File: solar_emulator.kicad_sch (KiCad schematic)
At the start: 37 parts, among them J1 USB_C_Receptacle, Q1 NMOS, Q2 NMOS, Q4 NMOS, Q5 NMOS, SW1 SW_Push, SW2 SW_Push, U1 ESP32-S3-WROOM-1, U2 LD1117S33TR_SOT223, U3 HIP4081AIPZ

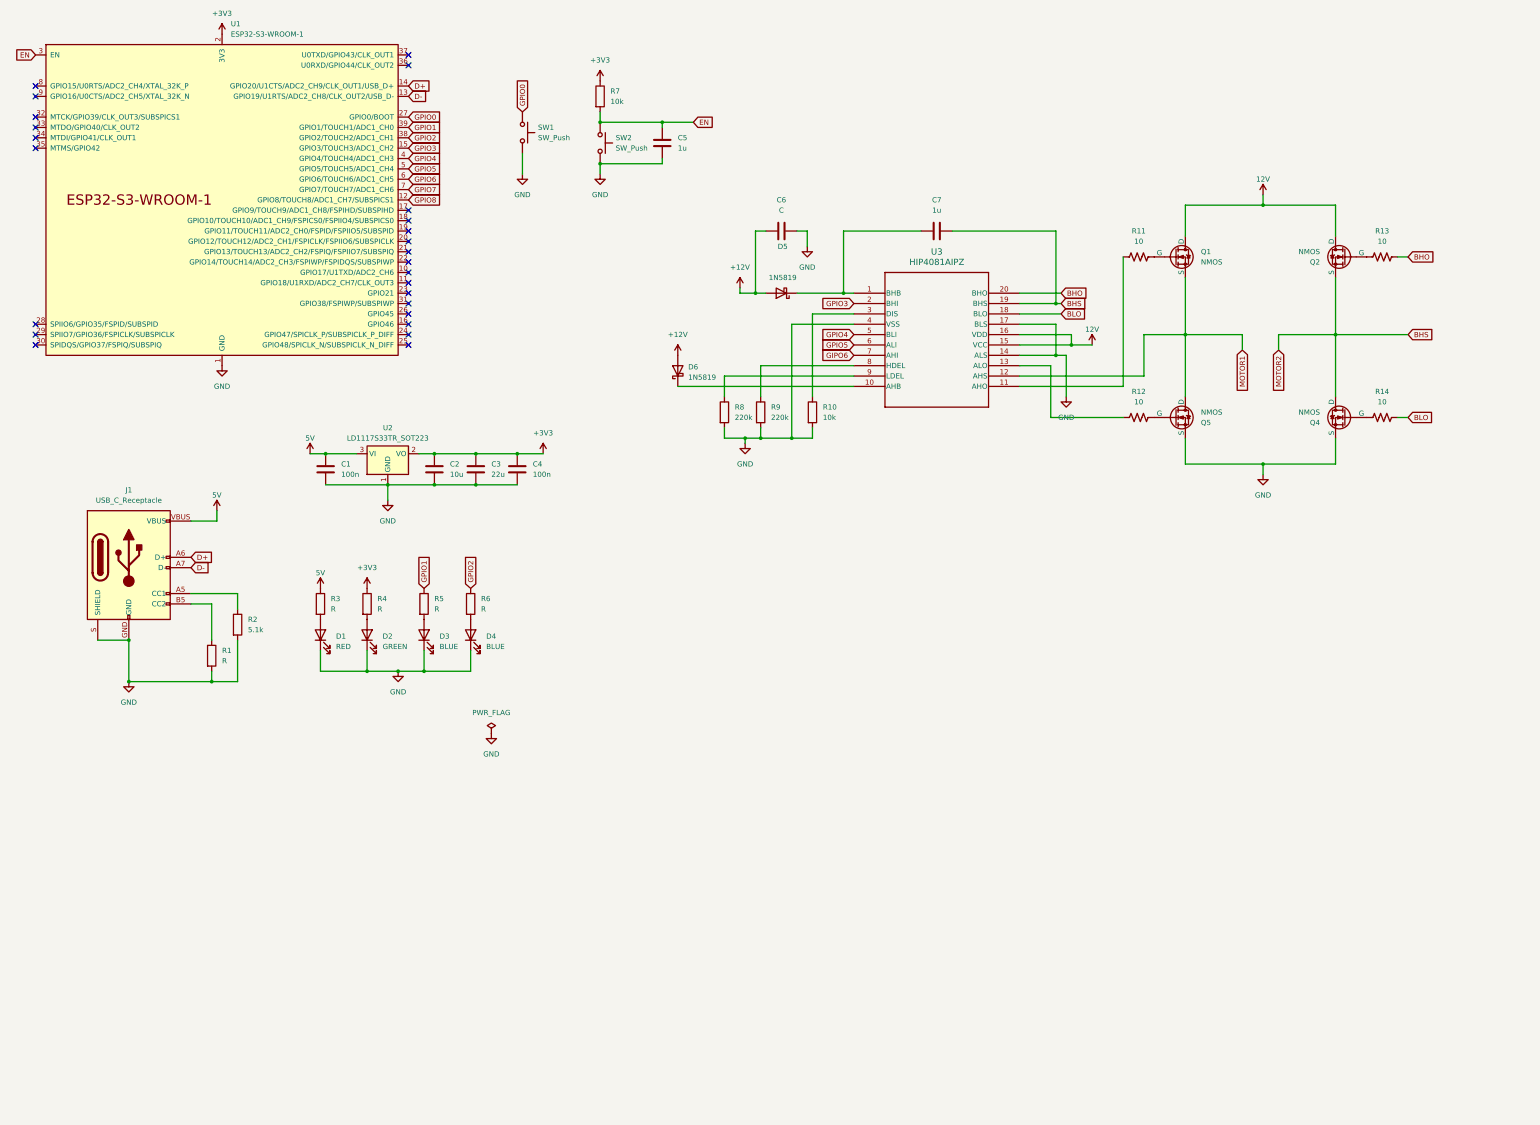
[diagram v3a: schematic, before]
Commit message: Schematic possibly complete, seek peer review
add another motor driver, barrel jack for +5V, pins for pwr mgmt
update LED indicators for pwr
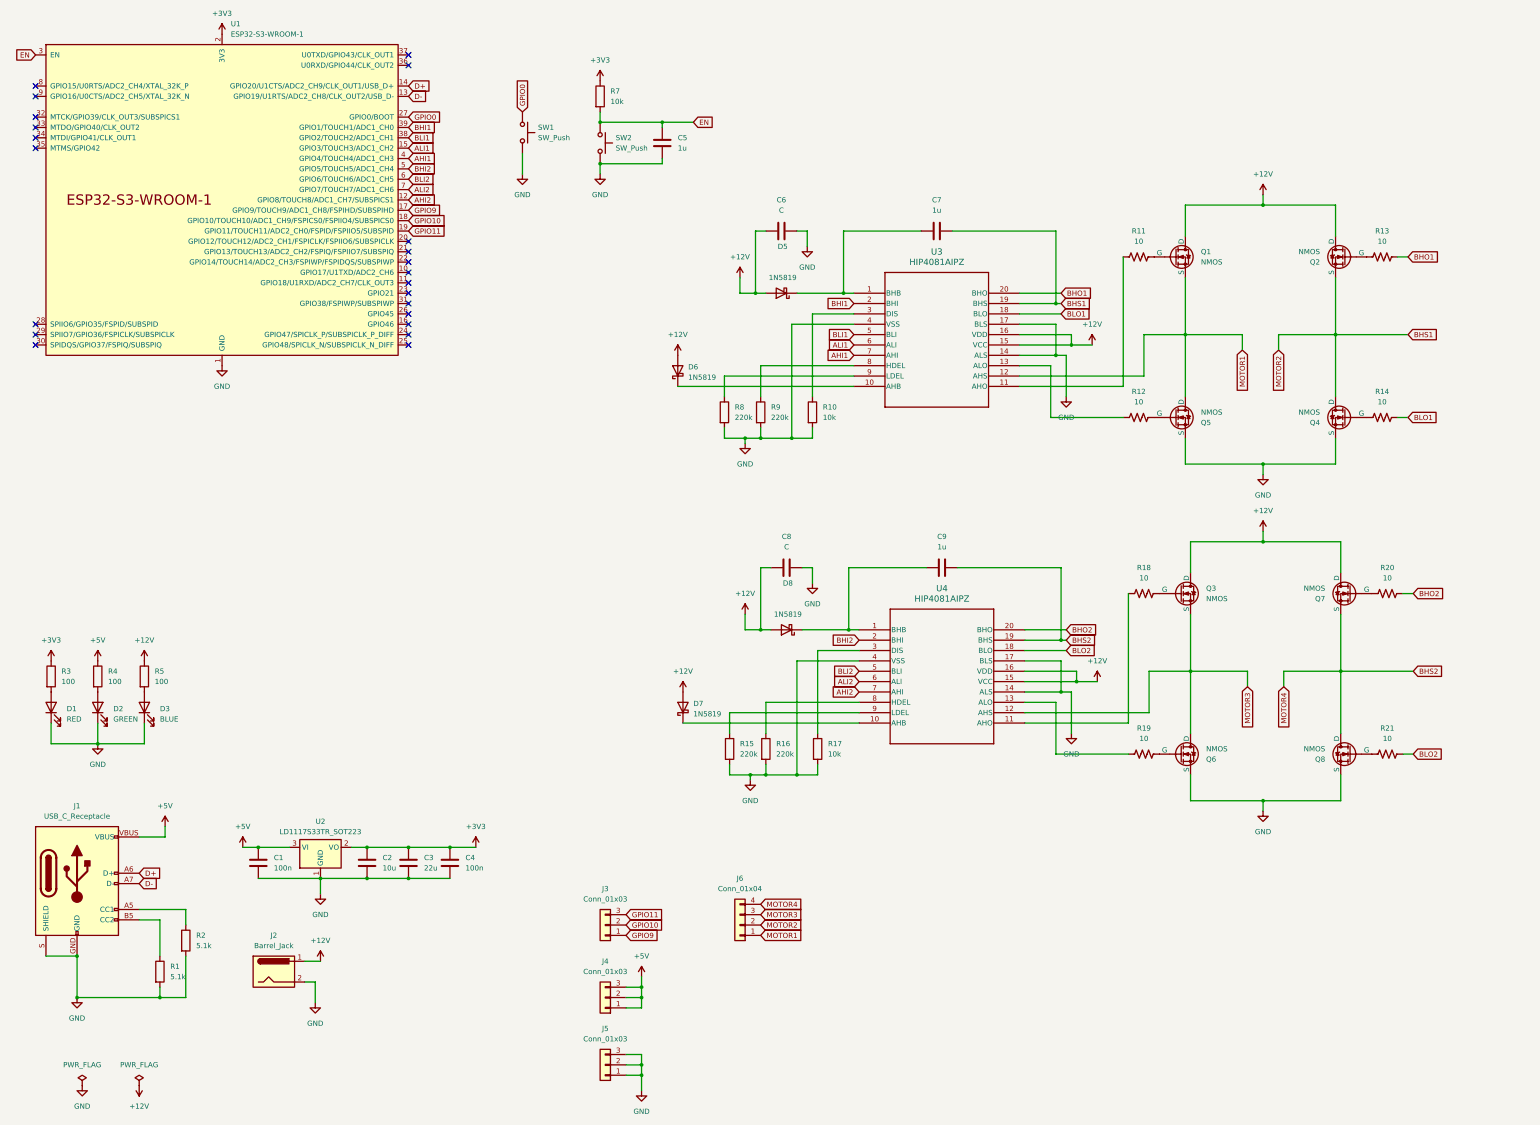
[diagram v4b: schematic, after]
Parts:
- removed D4: BLUE, symbol Device:LED
- removed R6: R, symbol Device:R
- added C8: C, symbol Device:C
- added C9: 1u, symbol Device:C
- added D7, D8: 1N5819, Diode_THT:D_DO-41_SOD81_P10.16mm_Horizontal, symbol Diode:1N5819
- added J2: Barrel_Jack, symbol Connector:Barrel_Jack
- added J3, J4, J5: Conn_01x03, symbol Connector_Generic:Conn_01x03
- added J6: Conn_01x04, symbol Connector_Generic:Conn_01x04
- added Q3, Q6, Q7, Q8: NMOS, symbol Simulation_SPICE:NMOS
- added R15, R16: 220k, symbol Device:R
- added R17: 10k, symbol Device:R
- added R18, R19, R20, R21: 10, SparkFun-Resistor:R_0603_1608Metric, symbol SparkFun-Resistor:R
- added U4: HIP4081AIPZ, PDIP20_7P11X26P9_INR, symbol custom_lib:HIP4081AIPZ
- R1: value R -> 5.1k
- R3, R4, R5: value R -> 100
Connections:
- net 12V is gone; now on net +12V: Q1.1 (D), Q2.1 (D), U3.15 (VCC), U3.16 (VDD)
- net +12V: now also R5.1, C8.1, D7.2 (A), D8.2 (A), J2.1, Q3.1 (D), Q7.1 (D), U4.15 (VCC), U4.16 (VDD)
- net +3V3: now also R3.1; no longer R4.1
- net GND: now also C8.2, J2.2, J5.1 (Pin_1), J5.2 (Pin_2), J5.3 (Pin_3), Q6.3 (S), Q8.3 (S), R15.2, R16.2, R17.2, U4.14 (ALS), U4.17 (BLS), U4.4 (VSS)
- net MOTOR1: now also J6.1 (Pin_1)
- net GPIO9: now reaches U1.17 (GPIO9/TOUCH9/ADC1_CH8/FSPIHD/SUBSPIHD)
- net GPIO9: now also J3.1 (Pin_1)
- net GPIO10: now reaches U1.18 (GPIO10/TOUCH10/ADC1_CH9/FSPICS0/FSPIIO4/SUBSPICS0)
- net GPIO10: now also J3.2 (Pin_2)
- net GPIO11: now reaches U1.19 (GPIO11/TOUCH11/ADC2_CH0/FSPID/FSPIIO5/SUBSPID)
- net GPIO11: now also J3.3 (Pin_3)
- net 5V renamed +5V
- net +5V: now also R4.1, J4.1 (Pin_1), J4.2 (Pin_2), J4.3 (Pin_3); no longer R3.1
- net BHO renamed BHO1
- net BHS renamed BHS1
- net BHS1: now also J6.2 (Pin_2)
- net BLO renamed BLO1
- net GIPO6 renamed AHI1
- net AHI1: now also U1.4 (GPIO4/TOUCH4/ADC1_CH3)
- net GPIO1 renamed BHI1
- net BHI1: now also U3.2 (BHI); no longer R5.1
- net GPIO2 renamed BLI1
- net BLI1: now also U3.5 (BLI)
- net GPIO3 renamed ALI1
- net ALI1: now also U3.6 (ALI); no longer U3.2 (BHI)
- removed net GPIO4: U1.4 (GPIO4/TOUCH4/ADC1_CH3), U3.5 (BLI)
- net GPIO5 renamed BHI2
- net BHI2: now also U4.2 (BHI); no longer U3.6 (ALI)
- net GPIO6 renamed BLI2
- net BLI2: now also U4.5 (BLI)
- net GPIO7 renamed ALI2
- net ALI2: now also U4.6 (ALI)
- net GPIO8 renamed AHI2
- net AHI2: now also U4.7 (AHI)
- new net: Q7.2 (G), R20.2
- new net: C9.1, D8.1 (K), U4.1 (BHB)
- new net: D7.1 (K), U4.10 (AHB)
- new net: R18.2, U4.11 (AHO)
- new net: R19.2, U4.13 (ALO)
- new net: R17.1, U4.3 (DIS)
- new net: R16.1, U4.8 (HDEL)
- new net: R15.1, U4.9 (LDEL)
- new net: Q6.2 (G), R19.1
- new net: Q8.2 (G), R21.2
- new net: Q3.2 (G), R18.1
- new net BHO2: R20.1, U4.20 (BHO)
- new net BHS2: C9.2, J6.4 (Pin_4), Q7.3 (S), Q8.1 (D), U4.19 (BHS)
- new net BLO2: R21.1, U4.18 (BLO)
- new net MOTOR3: J6.3 (Pin_3), Q3.3 (S), Q6.1 (D), U4.12 (AHS)
- no-connect marks 25 -> 22
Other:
- moved on the sheet: C1, C2, C3, C4, D1, D2, J1, R1, R2, R3, R4, U2

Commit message: update the jst connections on the schematic and some net list
will need to update the motor driver circuit, Jenny will
send the updates schematic later
Need to also assign footprints
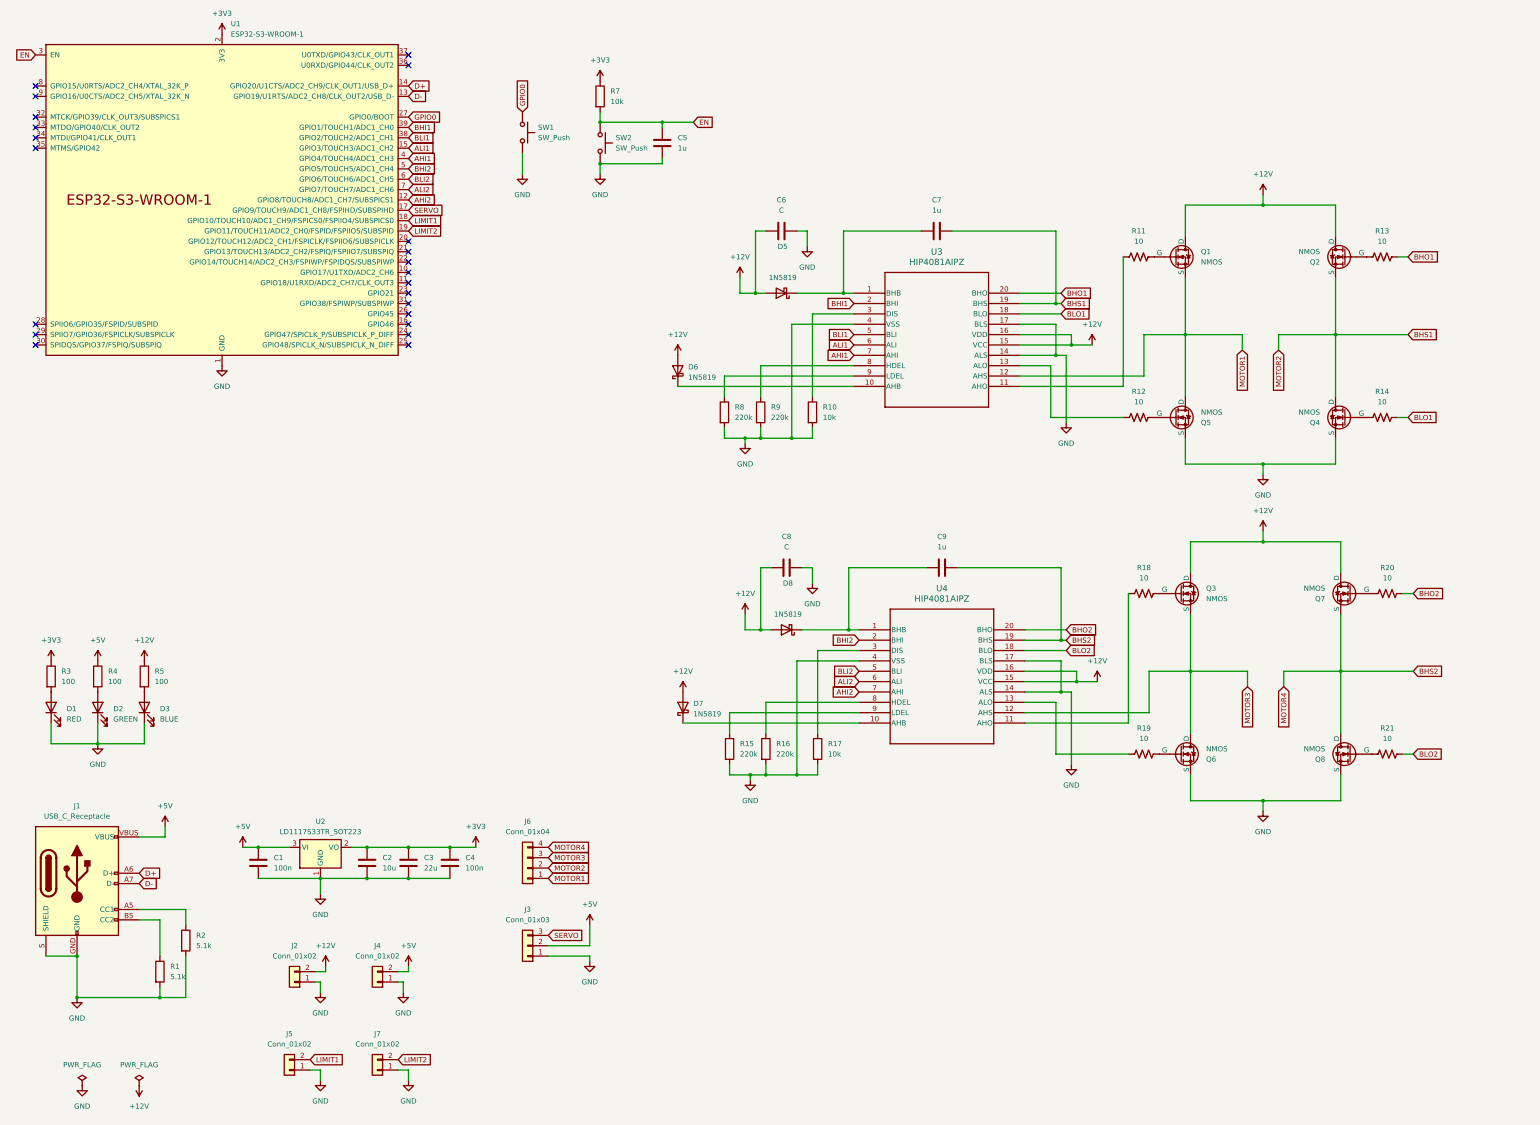
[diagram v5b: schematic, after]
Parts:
- removed J2: Barrel_Jack, symbol Connector:Barrel_Jack
- removed J4, J5: Conn_01x03, symbol Connector_Generic:Conn_01x03
- added J2, J4, J5, J7: Conn_01x02, symbol Connector_Generic:Conn_01x02
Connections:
- net +12V: now also J2.2 (Pin_2)
- net +5V: now also J3.2 (Pin_2), J4.2 (Pin_2)
- net GND: now also J3.1 (Pin_1), J2.1 (Pin_1), J4.1 (Pin_1), J5.1 (Pin_1), J7.1 (Pin_1)
- net GPIO10 renamed LIMIT1
- net LIMIT1: now also J5.2 (Pin_2); no longer J3.2 (Pin_2)
- net GPIO11 renamed LIMIT2
- net LIMIT2: now also J7.2 (Pin_2); no longer J3.3 (Pin_3)
- net GPIO9 renamed SERVO
- net SERVO: now also J3.3 (Pin_3); no longer J3.1 (Pin_1)
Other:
- moved on the sheet: J6
